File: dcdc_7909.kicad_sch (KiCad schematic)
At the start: 61 parts, among them J1 V_IN, J2 G_IN, J3 Conn_01x01, J4 Conn_01x01, J5 Conn_01x01, J6 Conn_01x01, J7 +10V, J8 G_OUT, J9 -10V, Q1 Si9435, U1 LM2940-SOT223-15, U2 MAX774, U3 LT3045xMSE, U4 LT3094xMSE

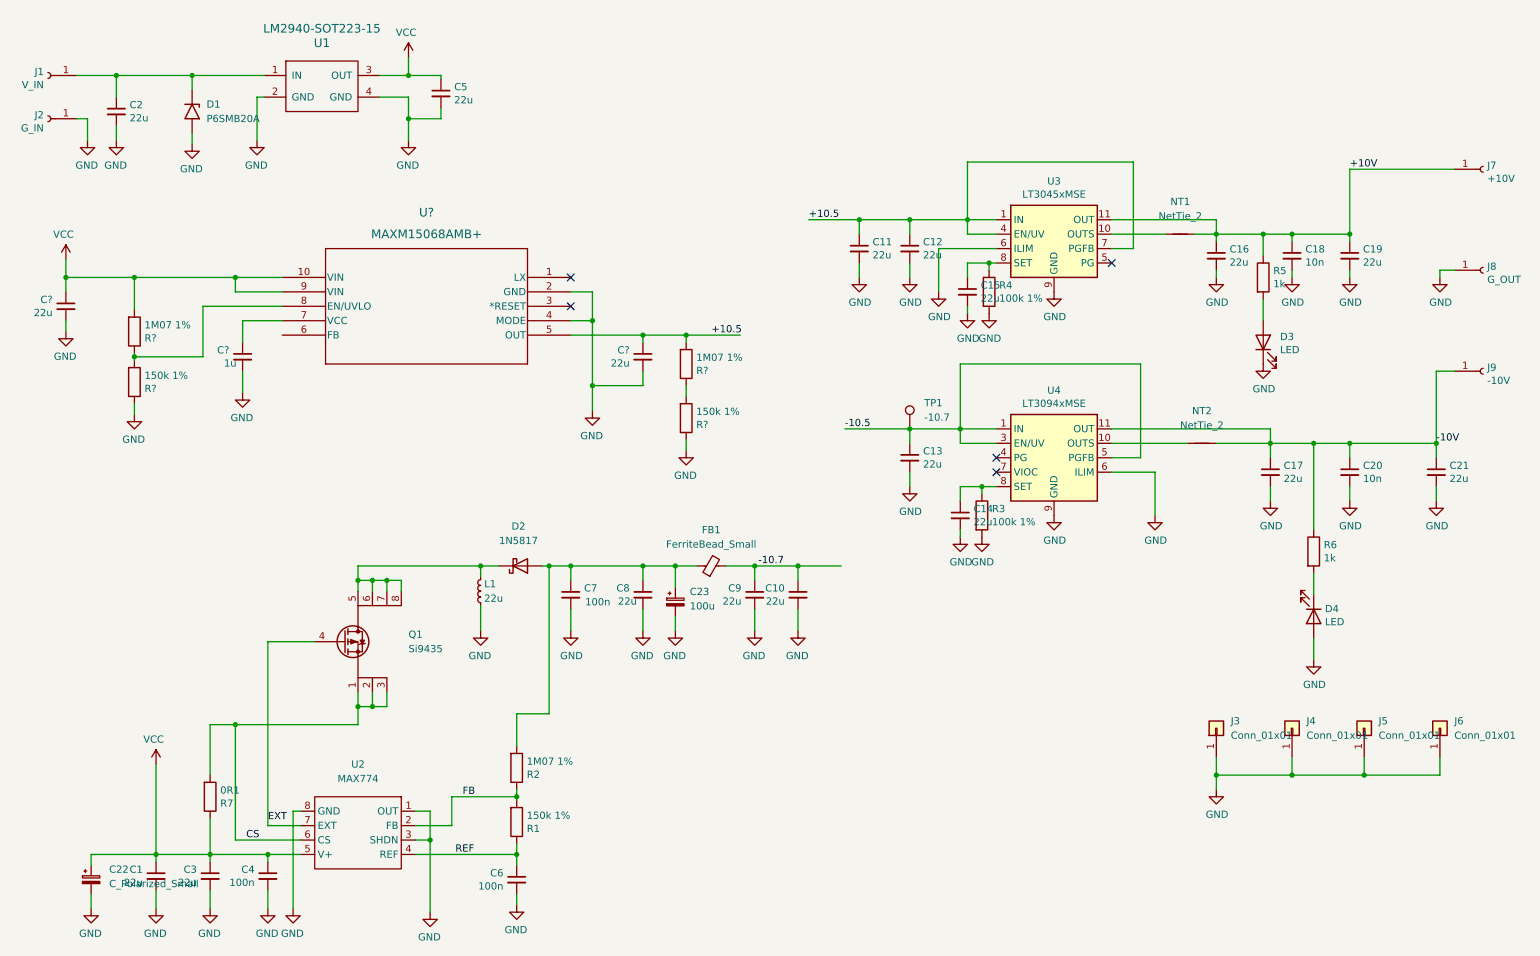
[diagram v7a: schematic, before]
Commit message: New version based on MAXM15068 and MAX17579.
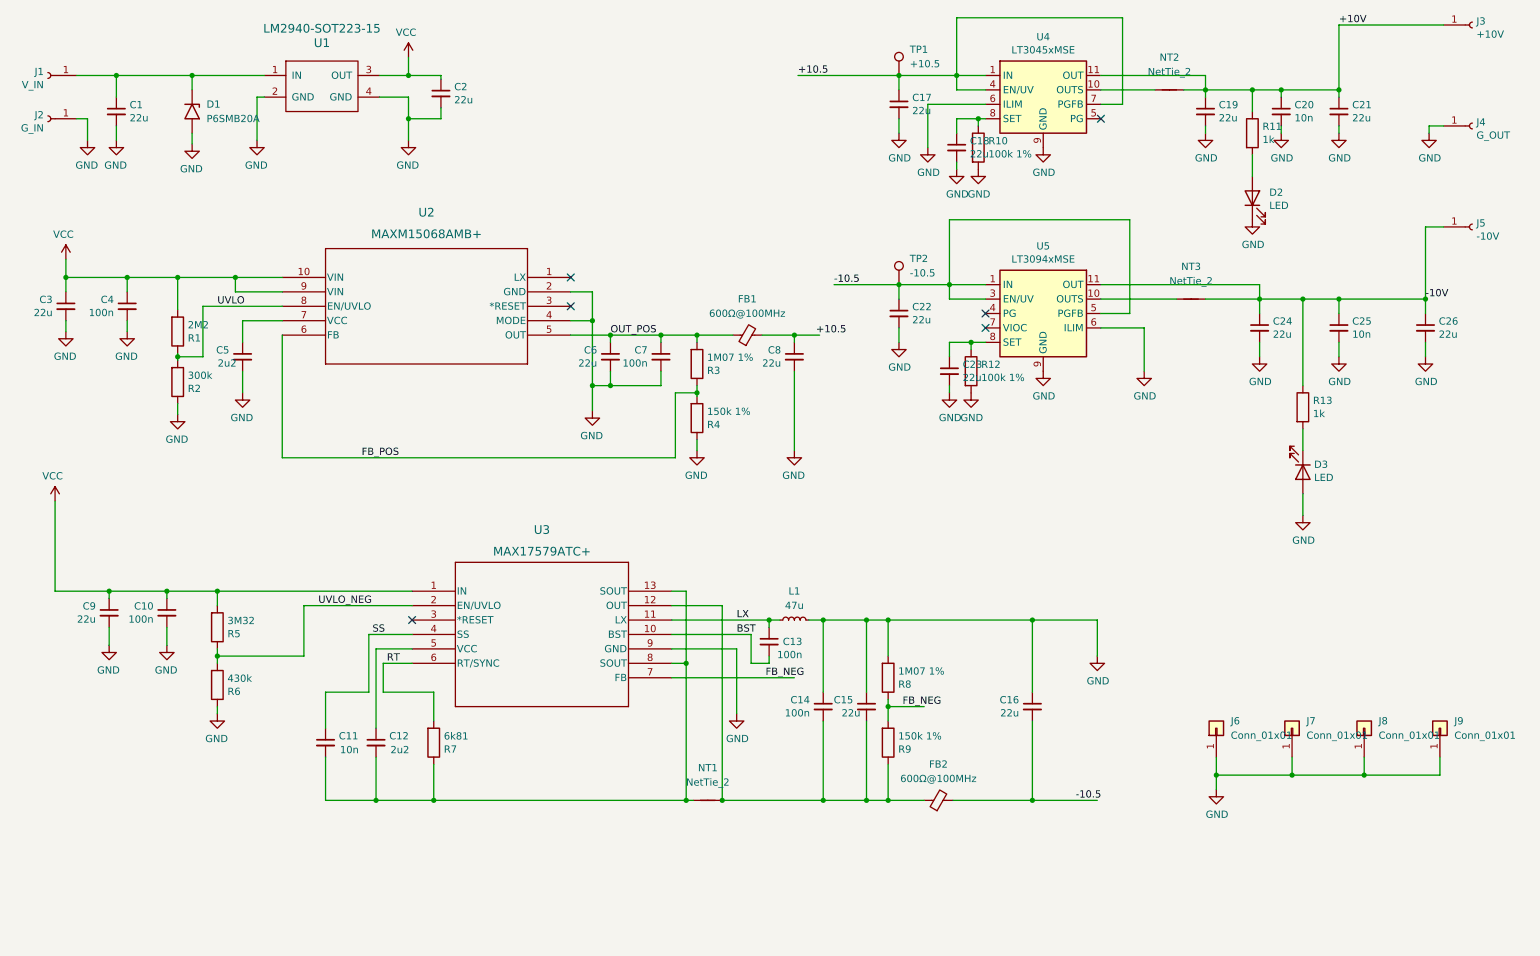
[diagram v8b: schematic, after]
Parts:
- removed C1, C10: 22u, Capacitor_SMD:C_1210_3225Metric, symbol Device:C_Small
- removed C22: C_Polarized_Small, Capacitor_Tantalum_SMD:CP_EIA-7343-31_Kemet-D_Pad2.25x2.55mm_HandSolder, symbol Device:C_Polarized_Small
- removed C23: 100u, Capacitor_Tantalum_SMD:CP_EIA-7343-31_Kemet-D_Pad2.25x2.55mm_HandSolder, symbol Device:C_Polarized_Small
- removed C6: 100n, Capacitor_SMD:C_0402_1005Metric, symbol Device:C_Small
- removed D2: 1N5817, Diode_SMD:D_PowerDI-123, symbol Diode:1N5817
- removed Q1: Si9435, Package_SO:SO-8_3.9x4.9mm_P1.27mm, symbol marcin_library:Si9435
- removed U2: MAX774, Package_SO:SO-8_3.9x4.9mm_P1.27mm, symbol marcin_library:MAX774
- added C12: 2u2, Capacitor_SMD:C_0805_2012Metric, symbol Device:C_Small
- added C13, C14, C4: 100n, Capacitor_SMD:C_0402_1005Metric, symbol Device:C_Small
- added C8: 22u, Capacitor_SMD:C_1210_3225Metric, symbol Device:C_Small
- added FB1: 600Ω@100MHz, Resistor_SMD:R_0805_2012Metric, symbol Device:FerriteBead_Small
- added NT1: NetTie_2, NetTie:NetTie-2_SMD_Pad0.5mm, symbol Device:NetTie_2
- added R5: 3M32, Resistor_SMD:R_0402_1005Metric, symbol Device:R
- added R6: 430k, Resistor_SMD:R_0402_1005Metric, symbol Device:R
- added TP1: +10.5, TestPoint:TestPoint_THTPad_D1.0mm_Drill0.5mm, symbol Connector:TestPoint
- added U3: MAX17579ATC+, marcin_library:21-0664_TD1233&plus_1C_MXM, symbol marcin_library:MAX17579ATC+
- C11: value 22u -> 10n; footprint Capacitor_SMD:C_1210_3225Metric -> Capacitor_SMD:C_0402_1005Metric; LCSC C426653 -> C15195; PN Murata GCM32EC71E226KE36 -> (none)
- C5: renamed from C?; value 1u -> 2u2; footprint Capacitor_SMD:C_1210_3225Metric -> Capacitor_SMD:C_0805_2012Metric
- FB2: renamed from FB1; value FerriteBead_Small -> 600Ω@100MHz
- L1: value 22u -> 47u; footprint Inductor_SMD:L_Coilcraft_XxL4040 -> Inductor_SMD:L_Coilcraft_XAL60xx_6.36x6.56mm
- R1: renamed from R?; value 1M07 1% -> 2M2
- R2: renamed from R?; value 150k 1% -> 300k
- R7: value 0R1 -> 6k81; footprint Resistor_SMD:R_0805_2012Metric -> Resistor_SMD:R_0402_1005Metric; LCSC C186573 -> C319870
- TP2: renamed from TP1; value -10.7 -> -10.5
- U2: renamed from U?; footprint 21-100094F_M102A3_1 -> marcin_library:10-eMGA (3x2.6)
- gave numbers to parts that had none: 4
- renumbered C2 to C1, C4 to C10, C8 to C15, C9 to C16, C12 to C17, C15 to C18, C16 to C19, C5 to C2, C18 to C20, C19 to C21, C13 to C22, C14 to C23, C17 to C24, C20 to C25, C21 to C26, C3 to C9, D3 to D2, D4 to D3, J7 to J3, J8 to J4, J9 to J5, J3 to J6, J4 to J7, J5 to J8, J6 to J9, NT1 to NT2, NT2 to NT3, R4 to R10, R5 to R11, R3 to R12, R6 to R13, R2 to R8, R1 to R9, U3 to U4, U4 to U5
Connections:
- net +10.5: now also C8.1, FB1.2, TP1.1; no longer C11.1, C6.1, R3.2, U2.5 (OUT)
- net -10.5: now also C16.2, FB2.2
- net GND: now also C15.1, C16.1, L1.1, R8.2, C14.1, C4.2, C8.2, R6.1, U3.9 (GND); no longer C11.2, C15.2, C16.2, L1.2
- net VCC: now also C4.1, R5.2, U3.1 (IN); no longer R7.1
- net UVLO: now reaches R1.1, R2.2, U2.8 (EN/UVLO)
- net FB_POS: now reaches U2.6 (FB)
- net FB_POS: now also R3.1, R4.2
- removed net -10.7: C16.1, FB2.2
- net CS renamed RT
- net RT: now also U3.6 (RT/SYNC)
- net FB renamed FB_NEG
- net FB_NEG: now also U3.7 (FB)
- net REF: no longer names the net of R9.1
- net REF: now also C15.2, FB2.1, C14.2, NT1.2, U3.12 (OUT)
- new net: C11.2, C12.2, NT1.1, R7.1, U3.13 (SOUT), U3.8 (SOUT)
- new net: C12.1, U3.5 (VCC)
- new net BST: C13.2, U3.10 (BST)
- new net LX: C13.1, L1.2, U3.11 (LX)
- new net OUT_POS: C6.1, C7.1, FB1.1, R3.2, U2.5 (OUT)
- new net SS: C11.1, U3.4 (SS)
- new net UVLO_NEG: R5.1, R6.2, U3.2 (EN/UVLO)
- no-connect marks 5 -> 6
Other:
- moved on the sheet: C10, C15, C16, C17, C18, C19, C20, C21, C22, C23, C24, C25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
